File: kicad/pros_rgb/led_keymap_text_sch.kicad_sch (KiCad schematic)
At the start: 0 parts

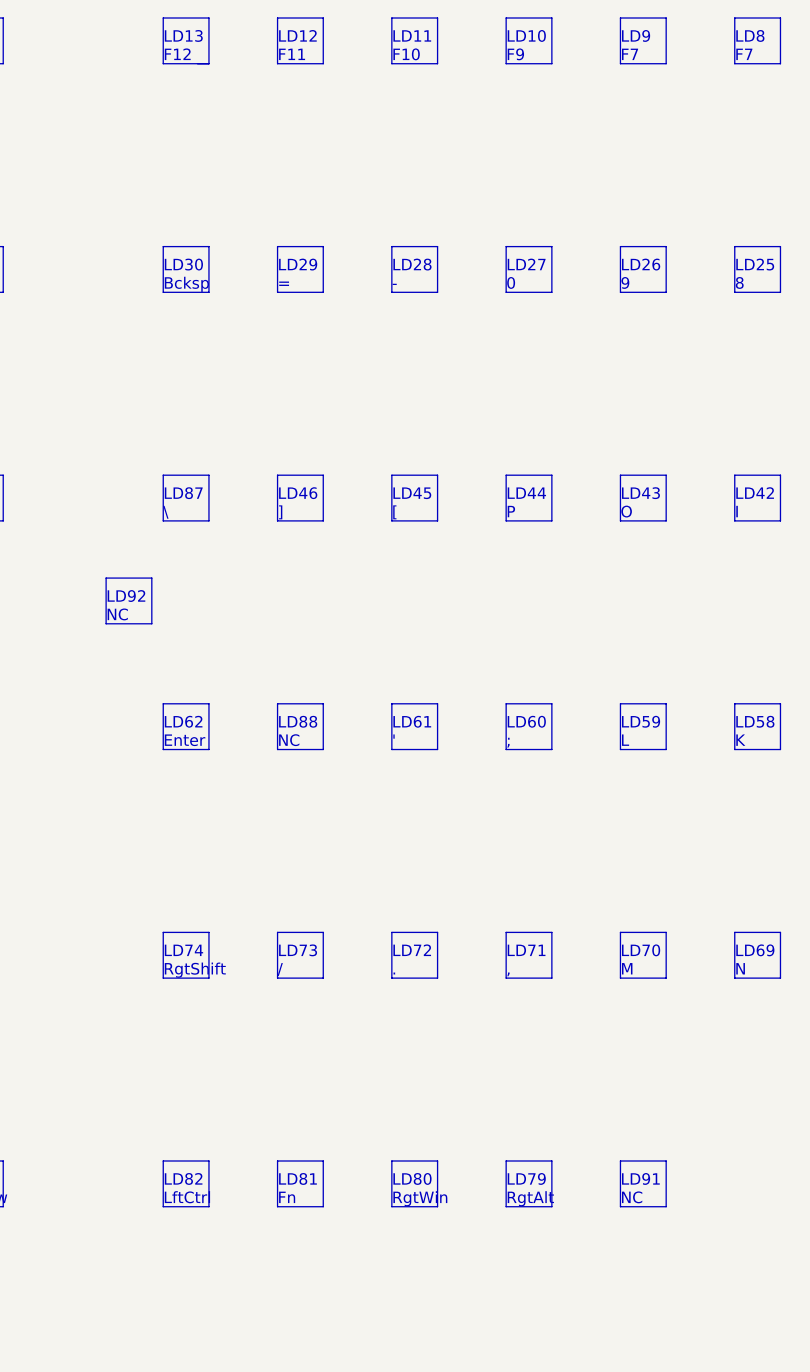
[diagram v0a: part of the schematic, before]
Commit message: kicad/pros_rgb: fix typos
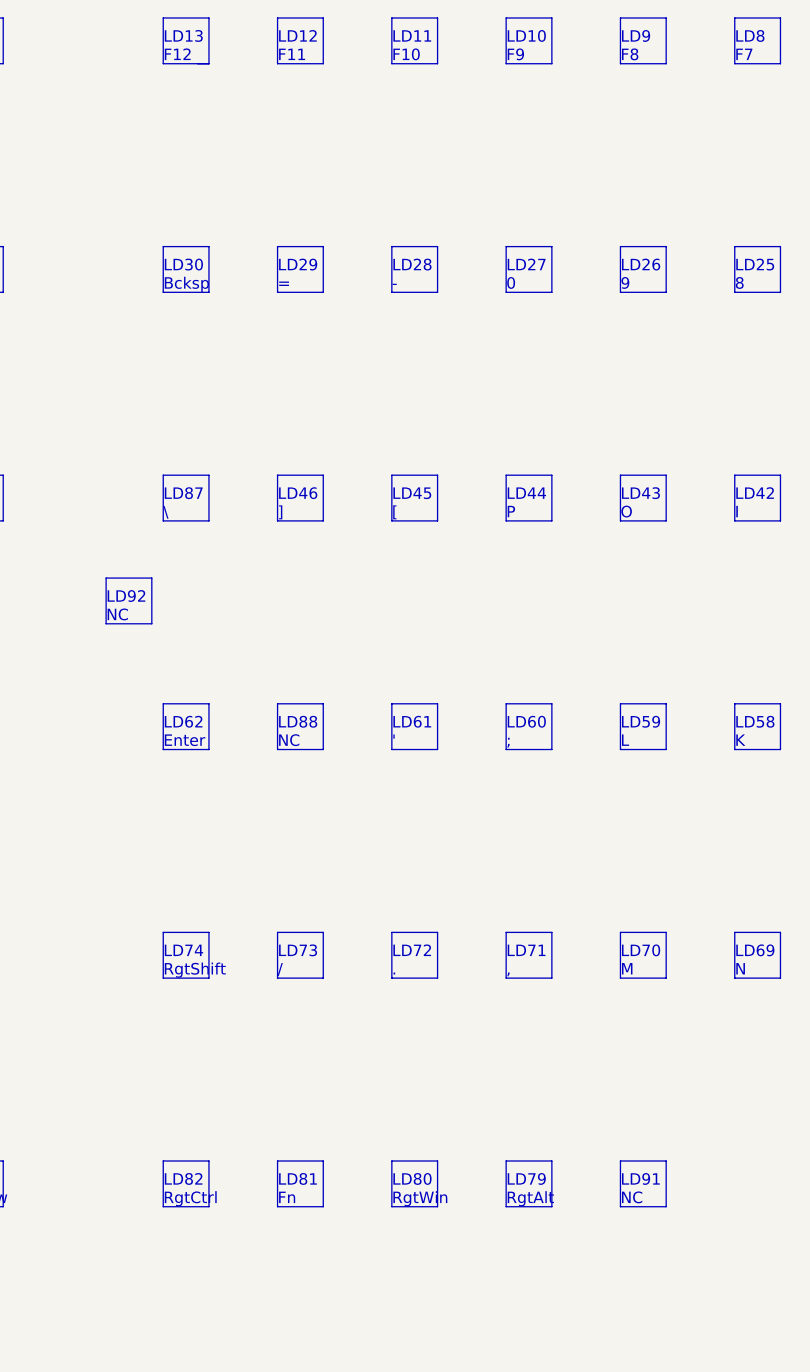
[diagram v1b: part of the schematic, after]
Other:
- note added: "LD82 RgtCtrl"
- note added: "LD9 F8"
- note removed: "LD82 LftCtrl"
- note removed: "LD9 F7"
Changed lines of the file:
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@@
     (effects (font (size 1.27 1.27)) (justify left bottom))
   )
-  (text "LD82\nLftCtrl" (at 88.9 158.75 0)
+  (text "LD82\nRgtCtrl" (at 88.9 158.75 0)
     (effects (font (size 1.27 1.27)) (justify left bottom))
   )
@@
     (effects (font (size 1.27 1.27)) (justify left bottom))
   )
-  (text "LD9\nF7" (at 139.7 31.75 0)
-    (effects (font (size 1.27 1.27)) (justify left bottom))
-  )
+  (text "LD9\nF8" (at 139.7 31.75 0)
+    (effects (font (size 1.27 1.27)) (justify left bottom))
+  )
